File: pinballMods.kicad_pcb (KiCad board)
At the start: 2 copper layers, 30.5 x 20.3 mm, 17 parts, among them J1 Conn_01x07_MountingPin, J2 Conn_02x07_Counter_Clockwise_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, J3 Conn_01x07_MountingPin

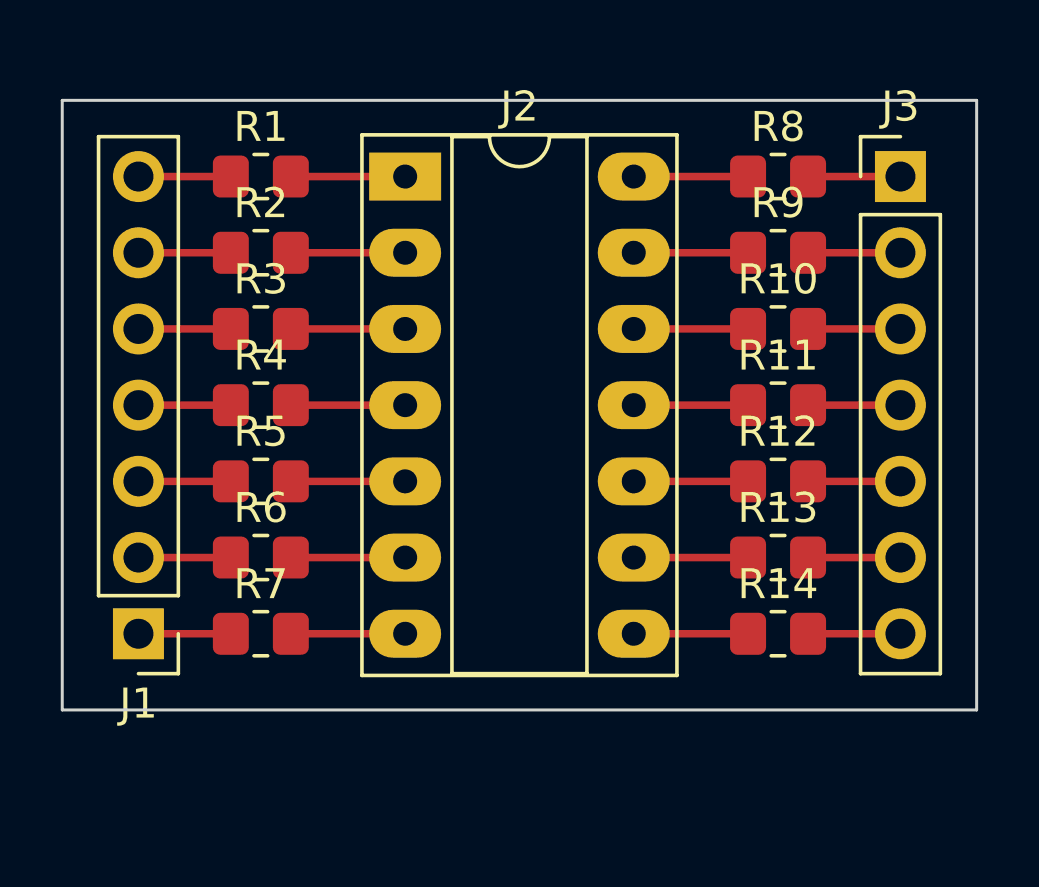
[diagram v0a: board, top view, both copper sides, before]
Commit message: Update To Socket and pins
Added DIP16 socket and extra set of pins and pads for 0805 0Ohm resistors.
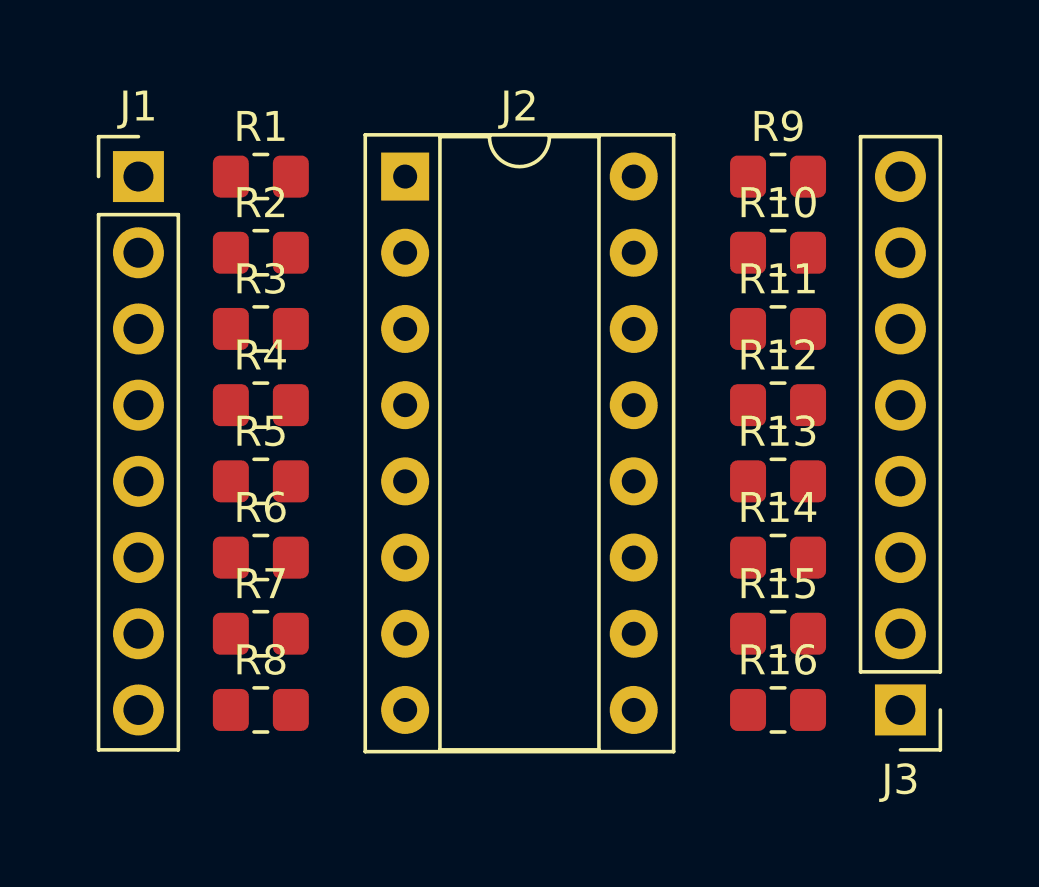
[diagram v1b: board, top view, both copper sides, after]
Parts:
- added R16: R_Small_US, Resistor_SMD:R_0805_2012Metric_Pad1.20x1.40mm_HandSolder, F.Cu at (167.4, 109.2)
- added R8: R_Small_US, Resistor_SMD:R_0805_2012Metric_Pad1.20x1.40mm_HandSolder, F.Cu at (150.1, 109.2)
- J1, J3: value Conn_01x07_MountingPin -> Conn_01x08_Male; footprint Connector_PinHeader_2.54mm:PinHeader_1x07_P2.54mm_Vertical -> Connector_PinHeader_2.54mm:PinHeader_1x08_P2.54mm_Vertical
- J2: value Conn_02x07_Counter_Clockwise_MountingPin -> Conn_02x08_Counter_Clockwise; footprint Package_DIP:DIP-14_W7.62mm_Socket_LongPads -> Package_DIP:DIP-16_W7.62mm_Socket
- R2: value R1 -> R2
- moved J3 17.8 mm to (171.4, 109.2), turned to 180 degrees
- moved J1 15.2 mm to (146.1, 91.4), turned to 0 degrees
- renumbered R9 to R10, R10 to R11, R11 to R12, R12 to R13, R13 to R14, R14 to R15, R8 to R9
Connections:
- R1 pad 1: Net-(J1-Pad7) -> Net-(J1-Pad1)
- R10 pad 1: Net-(J2-Pad13) -> Net-(J2-Pad15)
- R10 pad 2: Net-(J3-Pad2) -> Net-(J3-Pad7)
- R11 pad 1: Net-(J2-Pad12) -> Net-(J2-Pad14)
- R11 pad 2: Net-(J3-Pad3) -> Net-(J3-Pad6)
- R12 pad 1: Net-(J2-Pad11) -> Net-(J2-Pad13)
- R12 pad 2: Net-(J3-Pad4) -> Net-(J3-Pad5)
- R13 pad 1: Net-(J2-Pad10) -> Net-(J2-Pad12)
- R13 pad 2: Net-(J3-Pad5) -> Net-(J3-Pad4)
- R14 pad 1: Net-(J2-Pad9) -> Net-(J2-Pad11)
- R14 pad 2: Net-(J3-Pad6) -> Net-(J3-Pad3)
- R15 pad 1: Net-(J2-Pad8) -> Net-(J2-Pad10)
- R15 pad 2: Net-(J3-Pad7) -> Net-(J3-Pad2)
- R2 pad 1: Net-(J1-Pad6) -> Net-(J1-Pad2)
- R3 pad 1: Net-(J1-Pad5) -> Net-(J1-Pad3)
- R5 pad 1: Net-(J1-Pad3) -> Net-(J1-Pad5)
- R6 pad 1: Net-(J1-Pad2) -> Net-(J1-Pad6)
- R7 pad 1: Net-(J1-Pad1) -> Net-(J1-Pad7)
- R9 pad 1: Net-(J2-Pad14) -> Net-(J2-Pad16)
- R9 pad 2: Net-(J3-Pad1) -> Net-(J3-Pad8)
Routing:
- net Net-(J2-Pad9): track 3.81 -> 0.00 mm
- net Net-(J2-Pad8): track 3.81 -> 0.00 mm
- net Net-(J2-Pad7): track 3.81 -> 0.00 mm
- net Net-(J2-Pad6): track 3.81 -> 0.00 mm
- net Net-(J2-Pad5): track 3.81 -> 0.00 mm
- net Net-(J2-Pad4): track 3.81 -> 0.00 mm
- net Net-(J2-Pad3): track 3.81 -> 0.00 mm
- net Net-(J2-Pad2): track 3.81 -> 0.00 mm
- net Net-(J2-Pad14): track 3.81 -> 0.00 mm
- net Net-(J2-Pad13): track 3.81 -> 0.00 mm
- net Net-(J2-Pad12): track 3.81 -> 0.00 mm
- net Net-(J2-Pad11): track 3.81 -> 0.00 mm
- net Net-(J2-Pad10): track 3.81 -> 0.00 mm
- net Net-(J2-Pad1): track 3.81 -> 0.00 mm
- net Net-(J3-Pad7): track 3.08 -> 0.00 mm
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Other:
- board outline removed

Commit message: Minor changes
Widened through holes for sockets to .1in pitch and widened traces to .5mm
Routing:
- net Net-(J2-Pad9): track 0.00 -> 3.81 mm
- net Net-(J2-Pad8): track 0.00 -> 3.81 mm
- net Net-(J2-Pad7): track 0.00 -> 3.81 mm
- net Net-(J2-Pad6): track 0.00 -> 3.81 mm
- net Net-(J2-Pad5): track 0.00 -> 3.81 mm
- net Net-(J2-Pad4): track 0.00 -> 3.81 mm
- net Net-(J2-Pad3): track 0.00 -> 3.81 mm
- net Net-(J2-Pad2): track 0.00 -> 3.81 mm
- net Net-(J2-Pad16): track 0.00 -> 3.81 mm
- net Net-(J2-Pad15): track 0.00 -> 3.81 mm
- net Net-(J2-Pad14): track 0.00 -> 3.81 mm
- net Net-(J2-Pad13): track 0.00 -> 3.81 mm
- net Net-(J2-Pad12): track 0.00 -> 3.81 mm
- net Net-(J2-Pad11): track 0.00 -> 3.81 mm
- net Net-(J2-Pad10): track 0.00 -> 3.81 mm
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
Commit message: Edge Cuts
Added edge cuts
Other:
- board outline added: 30.5 x 25.4 mm

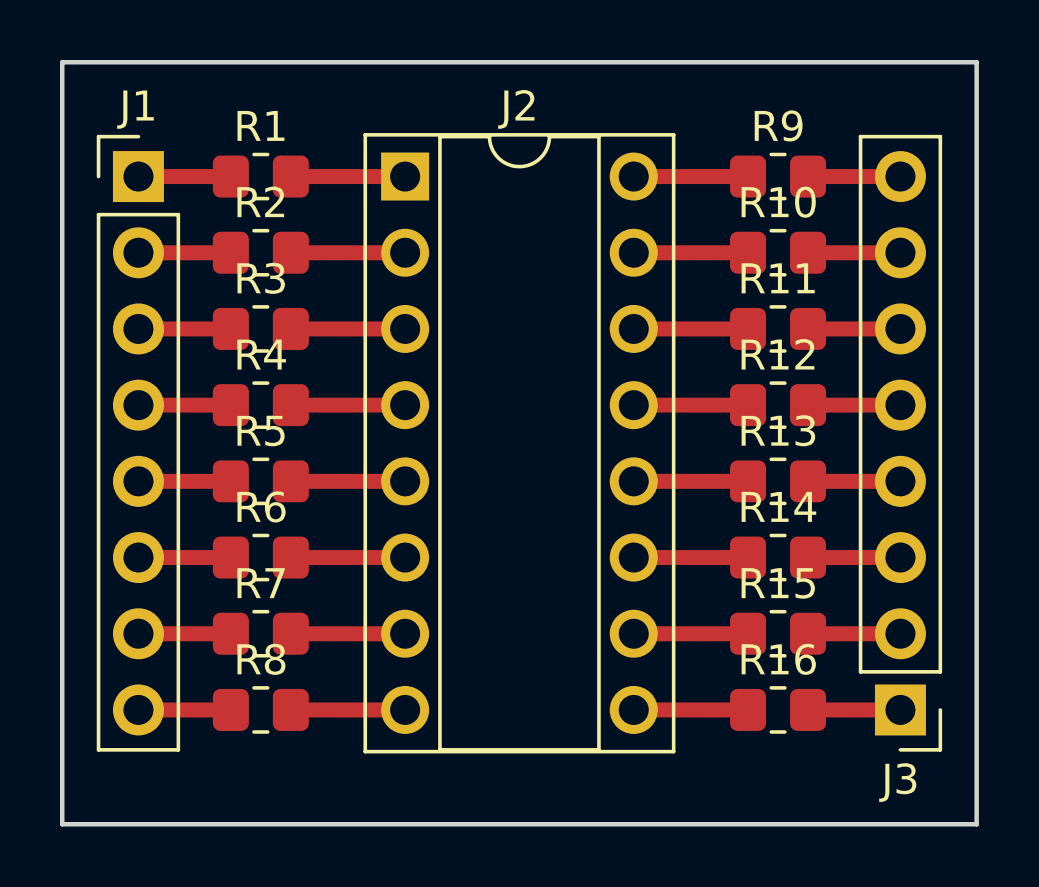
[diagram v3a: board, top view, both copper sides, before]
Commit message: Rev 2.1
Removed silkk screen text and shrunk board slightly.
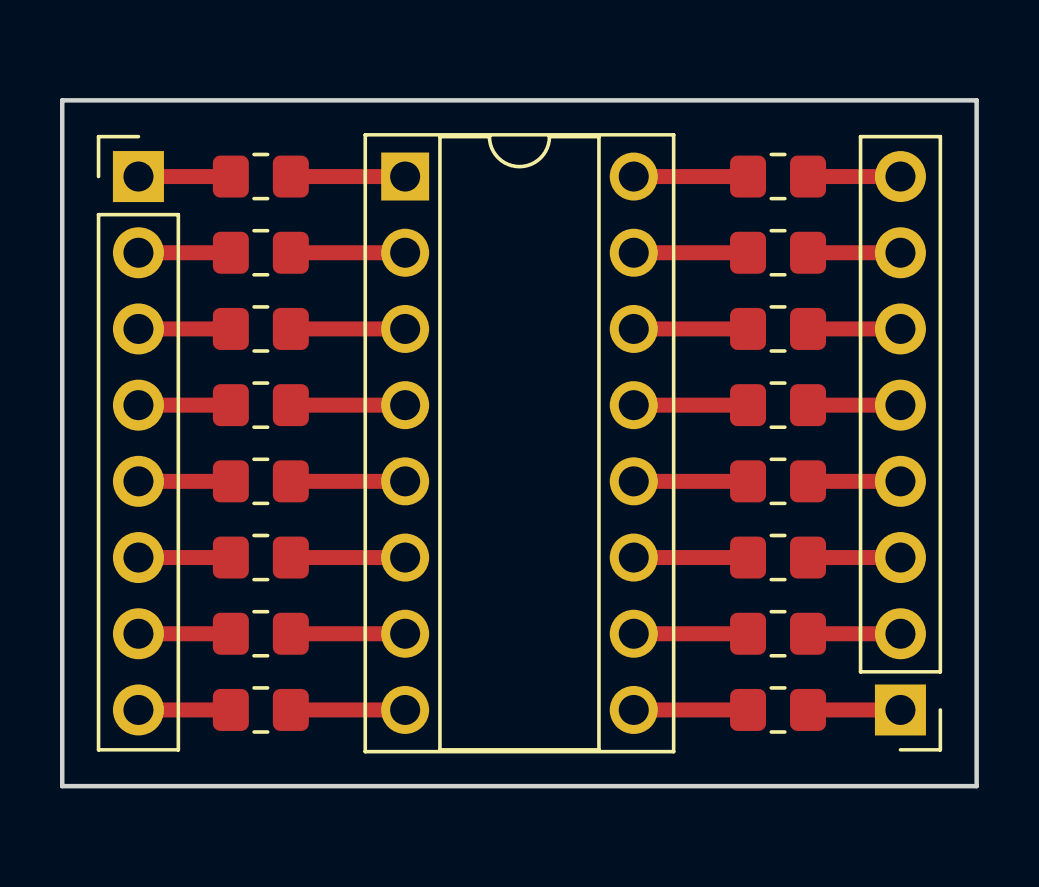
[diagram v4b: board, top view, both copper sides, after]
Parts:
- renumbered J3 to ?, R11 to ?, R10 to ?, R9 to ?, R7 to ?, R6 to ?, R5 to ?, R4 to ?, R3 to ?, R2 to ?, R1 to ?, J2 to ?, J1 to ?, R16 to ?, R8 to ?, R15 to ?, R14 to ?, R13 to ?, R12 to ?
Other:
- board size 30.5 x 25.4 mm -> 30.5 x 22.9 mm

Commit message: Rev 2.2
Added pin numbers, links, and rev to silk screens
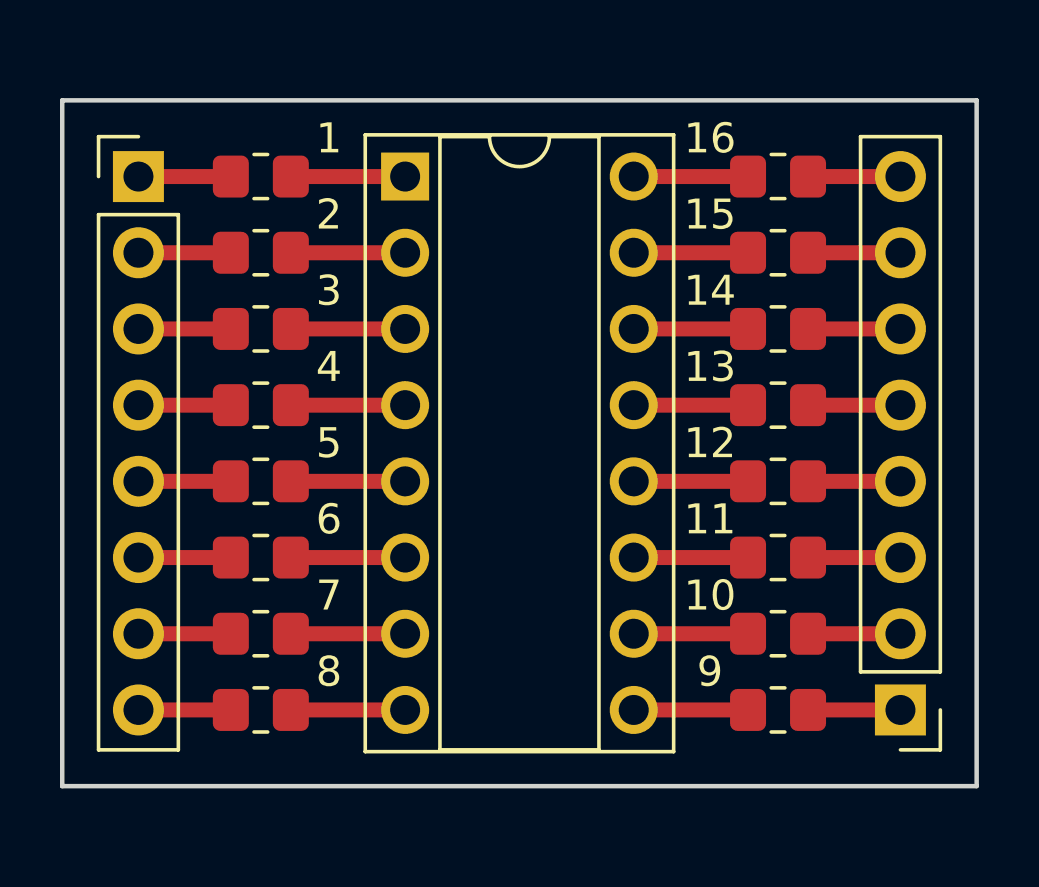
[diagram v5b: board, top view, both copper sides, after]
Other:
- board text added: "1"
- board text added: "10"
- board text added: "11"
- board text added: "12"
- board text added: "13"
- board text added: "14"
- board text added: "15"
- board text added: "16"
- board text added: "2"
- board text added: "3"
- board text added: "4"
- board text added: "5"
- board text added: "6"
- board text added: "7"
- board text added: "8"
- board text added: "9"
- board text added: "Rev 2.2"
- board text added: "https://github.com /Blacknight318/PinballMods"
- board text added: "https://www.youtube.com/ channel/ UCBChd470tGYKNLbeN0ta27g"
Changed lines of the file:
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@@
   (general
     (thickness 1.6)
-    (drawings 4)
+    (drawings 23)
     (tracks 32)
     (zones 0)
@@
     )
   )
+  (gr_text "https://github.com\n/Blacknight318/PinballMods" (at 158.75 100.33 90) (layer B.SilkS)
+    (effects (font (size 1 1) (thickness 0.2)) (justify mirror))
+  )
+  (gr_text "Rev 2.2" (at 167.64 100.33 90) (layer B.SilkS)
+    (effects (font (size 1.5 1.5) (thickness 0.3)) (justify mirror))
+  )
+  (gr_text "https://www.youtube.com/\nchannel/\nUCBChd470tGYKNLbeN0ta27g" (at 149.86 100.33 90) (layer B.SilkS)
+    (effects (font (size 1 1) (thickness 0.2)) (justify mirror))
+  )
+  (gr_text 16 (at 165.1 90.17) (layer F.SilkS)
+    (effects (font (size 1 1) (thickness 0.25)))
+  )
+  (gr_text 15 (at 165.1 92.71) (layer F.SilkS)
+    (effects (font (size 1 1) (thickness 0.25)))
+  )
+  (gr_text 14 (at 165.1 95.25) (layer F.SilkS)
+    (effects (font (size 1 1) (thickness 0.25)))
+  )
+  (gr_text 13 (at 165.1 97.79) (layer F.SilkS)
+    (effects (font (size 1 1) (thickness 0.25)))
+  )
+  (gr_text 12 (at 165.1 100.33) (layer F.SilkS)
+    (effects (font (size 1 1) (thickness 0.25)))
+  )
+  (gr_text 11 (at 165.1 102.87) (layer F.SilkS)
+    (effects (font (size 1 1) (thickness 0.25)))
+  )
+  (gr_text 10 (at 165.1 105.41) (layer F.SilkS)
+    (effects (font (size 1 1) (thickness 0.25)))
+  )
+  (gr_text 9 (at 165.1 107.95) (layer F.SilkS)
+    (effects (font (size 1 1) (thickness 0.25)))
+  )
+  (gr_text 8 (at 152.4 107.95) (layer F.SilkS)
+    (effects (font (size 1 1) (thickness 0.25)))
+  )
+  (gr_text 7 (at 152.4 105.41) (layer F.SilkS)
+    (effects (font (size 1 1) (thickness 0.25)))
+  )
+  (gr_text 6 (at 152.4 102.87) (layer F.SilkS)
+    (effects (font (size 1 1) (thickness 0.25)))
+  )
+  (gr_text 5 (at 152.4 100.33) (layer F.SilkS)
+    (effects (font (size 1 1) (thickness 0.25)))
+  )
+  (gr_text 4 (at 152.4 97.79) (layer F.SilkS)
+    (effects (font (size 1 1) (thickness 0.25)))
+  )
+  (gr_text 3 (at 152.4 95.25) (layer F.SilkS)
+    (effects (font (size 1 1) (thickness 0.25)))
+  )
+  (gr_text 2 (at 152.4 92.71) (layer F.SilkS)
+    (effects (font (size 1 1) (thickness 0.25)))
+  )
+  (gr_text 1 (at 152.4 90.17) (layer F.SilkS)
+    (effects (font (size 1 1) (thickness 0.25)))
+  )
   (gr_line (start 143.51 111.76) (end 143.51 88.9) (layer Edge.Cuts) (width 0.15))
